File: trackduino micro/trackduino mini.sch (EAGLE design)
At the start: 28 parts, among them IC2 74AHC1G125DBV, SW1 SPST_TACT-KMR2, U1 ATMEGA168, Y1 16MHZ

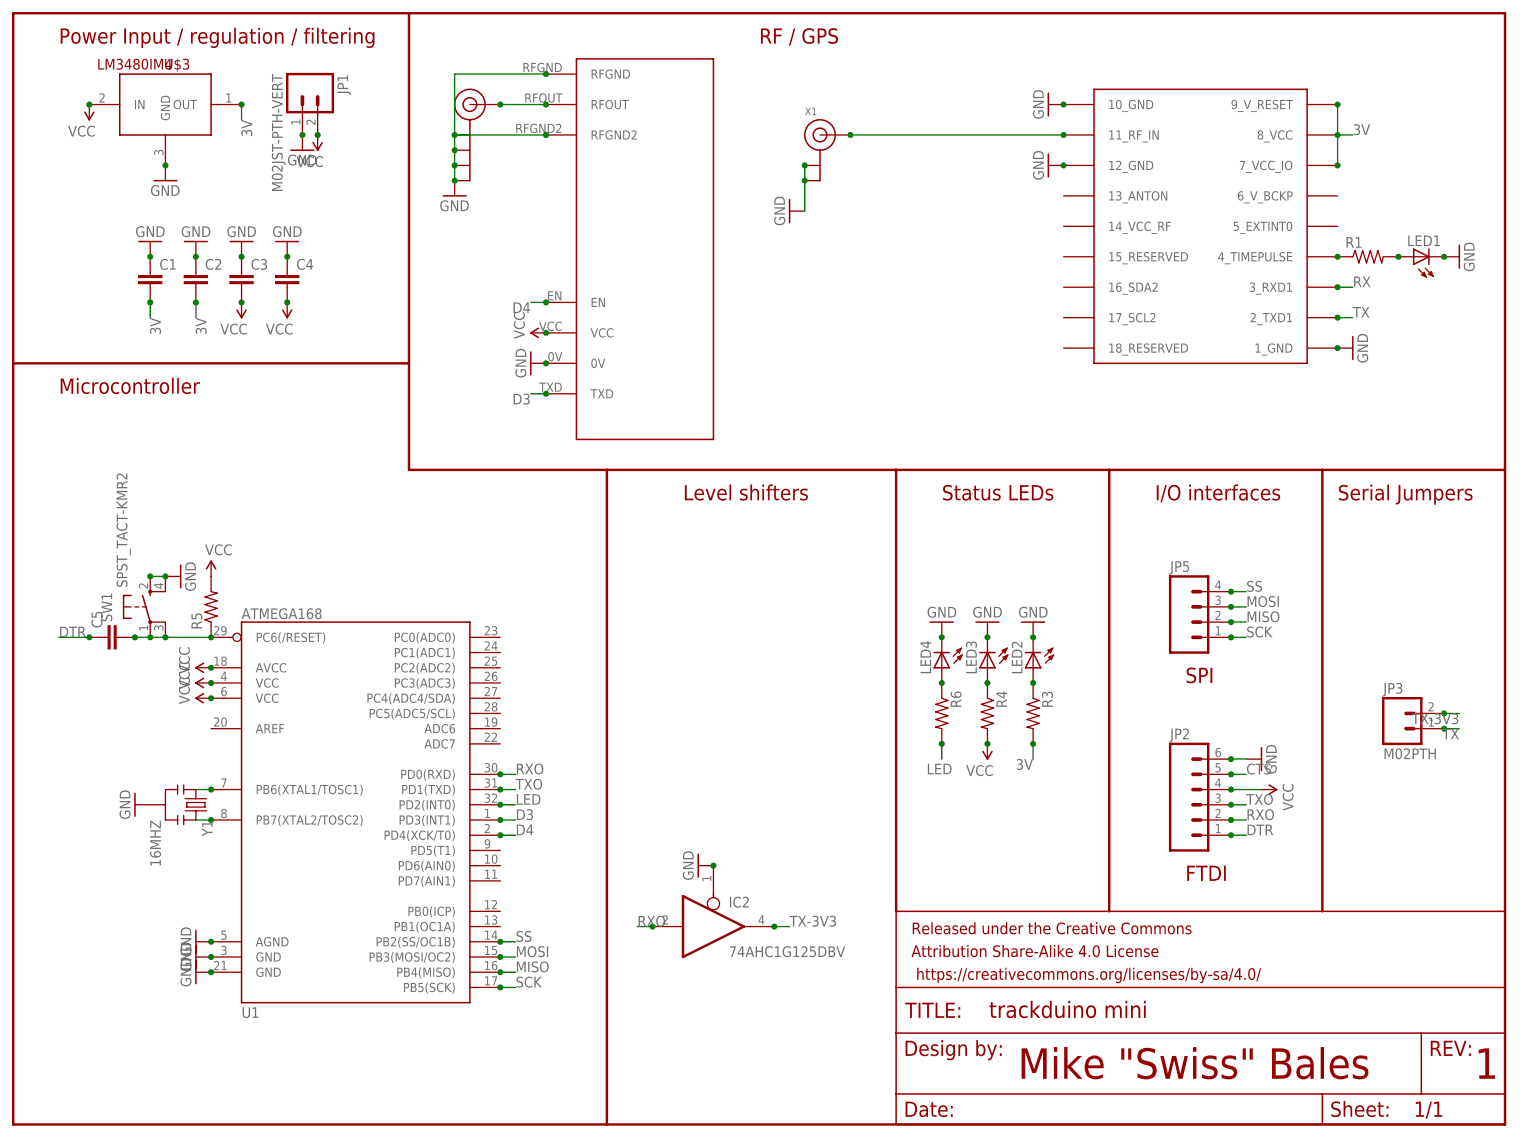
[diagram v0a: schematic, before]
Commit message: Revert 8864008..107cc9b
This rolls back to commit 8864008ccbdc4df3da8dbd79e6a63e8a5caf342f.
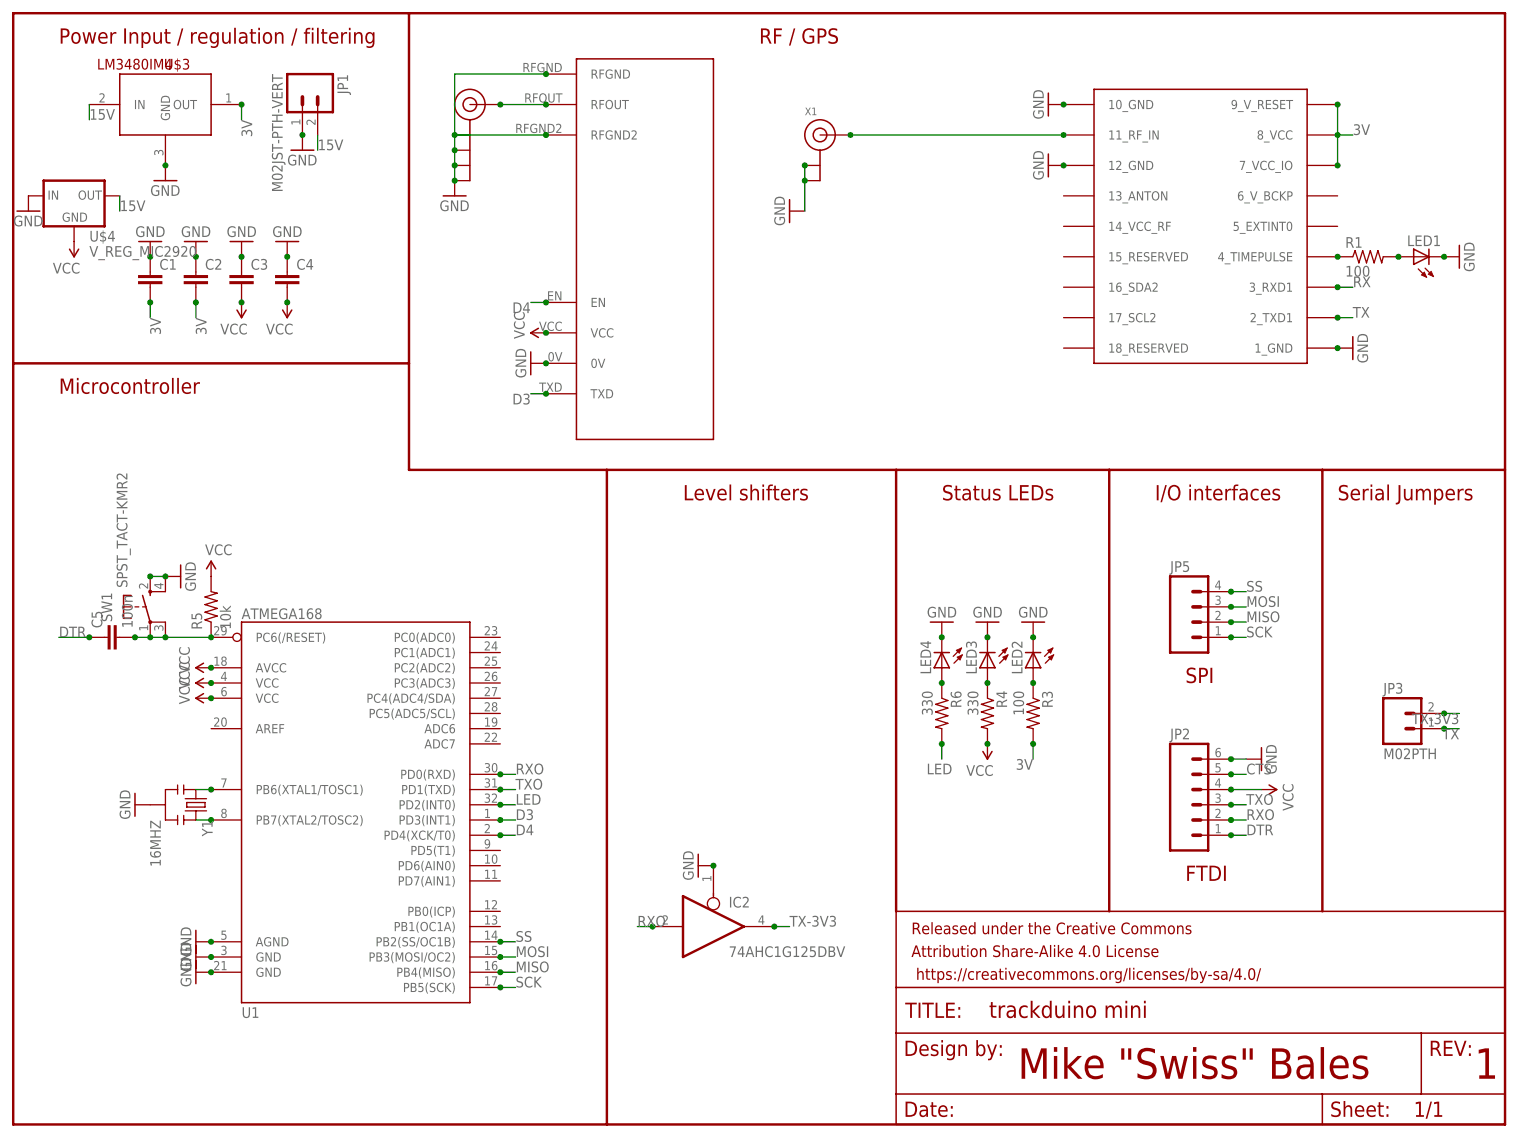
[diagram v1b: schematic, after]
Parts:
- added U$4: V_REG_MIC2920, SparkFun-PowerIC:V_REG_MIC2920
- C5: value (none) -> 100n
- R1, R3: value (none) -> 100
- R4, R6: value (none) -> 330
- R5: value (none) -> 10k
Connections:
- new net 15V: JP1.2, U$3.IN, U$4.OUT
- net GND: now also U$4.IN
- net VCC: now also U$4.GND; no longer JP1.2, U$3.IN
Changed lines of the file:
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@@
 <part name="GND4" library="SparkFun-Aesthetics" deviceset="GND" device=""/>
 <part name="GND5" library="SparkFun-Aesthetics" deviceset="GND" device=""/>
-<part name="SUPPLY1" library="SparkFun-Aesthetics" deviceset="VCC" device=""/>
-<part name="SUPPLY2" library="SparkFun-Aesthetics" deviceset="VCC" device=""/>
 <part name="SUPPLY3" library="SparkFun-Aesthetics" deviceset="VCC" device=""/>
 <part name="GND7" library="SparkFun-Aesthetics" deviceset="GND" device=""/>
-<part name="R1" library="SparkFun-Resistors" deviceset="RESISTOR" device="0805-RES"/>
+<part name="R1" library="SparkFun-Resistors" deviceset="RESISTOR" device="0805-RES" value="100"/>
 <part name="LED1" library="adafruit" deviceset="LED" device="CHIP-LED0805"/>
 <part name="GND8" library="SparkFun-Aesthetics" deviceset="GND" device=""/>
@@
 <part name="SUPPLY5" library="SparkFun-Aesthetics" deviceset="VCC" device=""/>
 <part name="LED2" library="adafruit" deviceset="LED" device="CHIP-LED0805"/>
-<part name="R3" library="SparkFun-Resistors" deviceset="RESISTOR" device="0805-RES"/>
+<part name="R3" library="SparkFun-Resistors" deviceset="RESISTOR" device="0805-RES" value="100"/>
 <part name="LED3" library="adafruit" deviceset="LED" device="CHIP-LED0805"/>
-<part name="R4" library="SparkFun-Resistors" deviceset="RESISTOR" device="0805-RES"/>
+<part name="R4" library="SparkFun-Resistors" deviceset="RESISTOR" device="0805-RES" value="330"/>
 <part name="GND19" library="SparkFun-Aesthetics" deviceset="GND" device=""/>
 <part name="GND20" library="SparkFun-Aesthetics" deviceset="GND" device=""/>
@@
 <part name="GND22" library="SparkFun-Aesthetics" deviceset="GND" device=""/>
 <part name="SUPPLY9" library="SparkFun-Aesthetics" deviceset="VCC" device=""/>
-<part name="R5" library="SparkFun-Resistors" deviceset="RESISTOR" device="0805-RES"/>
+<part name="R5" library="SparkFun-Resistors" deviceset="RESISTOR" device="0805-RES" value="10k"/>
 <part name="SUPPLY10" library="SparkFun-Aesthetics" deviceset="VCC" device=""/>
-<part name="C5" library="SparkFun-Capacitors" deviceset="CAP" device="0805"/>
+<part name="C5" library="SparkFun-Capacitors" deviceset="CAP" device="0805" value="100n"/>
 <part name="JP3" library="SparkFun-Connectors" deviceset="M02" device="PTH"/>
 <part name="JP5" library="SparkFun-Connectors" deviceset="M04" device="1X04_NO_SILK"/>
@@
 <part name="GND25" library="SparkFun-Aesthetics" deviceset="GND" device=""/>
 <part name="LED4" library="adafruit" deviceset="LED" device="CHIP-LED0805"/>
-<part name="R6" library="SparkFun-Resistors" deviceset="RESISTOR" device="0805-RES"/>
+<part name="R6" library="SparkFun-Resistors" deviceset="RESISTOR" device="0805-RES" value="330"/>
 <part name="GND26" library="SparkFun-Aesthetics" deviceset="GND" device=""/>
 <part name="GND24" library="SparkFun-Aesthetics" deviceset="GND" device=""/>
@@
 <part name="GND1" library="SparkFun-Aesthetics" deviceset="GND" device=""/>
 <part name="GND3" library="SparkFun-Aesthetics" deviceset="GND" device=""/>
+<part name="U$4" library="SparkFun-PowerIC" deviceset="V_REG_MIC2920" device=""/>
+<part name="SUPPLY12" library="SparkFun-Aesthetics" deviceset="VCC" device=""/>
+<part name="GND6" library="SparkFun-Aesthetics" deviceset="GND" device=""/>
 </parts>
 <sheets>
@@
 <instance part="GND4" gate="1" x="73.66" y="154.94"/>
 <instance part="GND5" gate="1" x="48.26" y="162.56"/>
-<instance part="SUPPLY1" gate="G$1" x="50.8" y="165.1" rot="R180"/>
-<instance part="SUPPLY2" gate="G$1" x="12.7" y="170.18" rot="R180"/>
 <instance part="SUPPLY3" gate="G$1" x="88.9" y="132.08" rot="R90"/>
 <instance part="GND7" gate="1" x="86.36" y="127" rot="R270"/>
@@
 <instance part="GND1" gate="1" x="30.48" y="147.32" rot="R180"/>
 <instance part="GND3" gate="1" x="25.4" y="157.48"/>
+<instance part="U$4" gate="G$1" x="10.16" y="154.94"/>
+<instance part="SUPPLY12" gate="G$1" x="10.16" y="147.32" rot="R180"/>
+<instance part="GND6" gate="1" x="2.54" y="152.4"/>
 </instances>
 <busses>
@@
 <junction x="25.4" y="160.02"/>
 </segment>
+<segment>
+<pinref part="U$4" gate="G$1" pin="IN"/>
+<pinref part="GND6" gate="1" pin="GND"/>
+</segment>
 </net>
 <net name="TX-3V3" class="0">
@@
 <net name="VCC" class="0">
 <segment>
-<pinref part="U$3" gate="G$1" pin="IN"/>
-<pinref part="SUPPLY2" gate="G$1" pin="VCC"/>
-<junction x="12.7" y="170.18"/>
-</segment>
-<segment>
-<pinref part="JP1" gate="G$1" pin="2"/>
-<pinref part="SUPPLY1" gate="G$1" pin="VCC"/>
-<junction x="50.8" y="165.1"/>
-</segment>
-<segment>
 <pinref part="U$2" gate="G$1" pin="VCC"/>
 <pinref part="SUPPLY3" gate="G$1" pin="VCC"/>
@@
 <pinref part="SUPPLY11" gate="G$1" pin="VCC"/>
 <junction x="33.02" y="76.2"/>
+</segment>
+<segment>
+<pinref part="U$4" gate="G$1" pin="GND"/>
+<pinref part="SUPPLY12" gate="G$1" pin="VCC"/>
 </segment>
 </net>
@@
 </segment>
 </net>
+<net name="15V" class="0">
+<segment>
+<pinref part="U$3" gate="G$1" pin="IN"/>
+<wire x1="12.7" y1="170.18" x2="12.7" y2="167.64" width="0.1524" layer="91"/>
+<label x="12.7" y="167.64" size="1.778" layer="95"/>
+</segment>
+<segment>
+<pinref part="JP1" gate="G$1" pin="2"/>
+<wire x1="50.8" y1="165.1" x2="50.8" y2="162.56" width="0.1524" layer="91"/>
+<label x="50.8" y="162.56" size="1.778" layer="95"/>
+</segment>
+<segment>
+<pinref part="U$4" gate="G$1" pin="OUT"/>
+<wire x1="17.78" y1="154.94" x2="17.78" y2="152.4" width="0.1524" layer="91"/>
+<label x="17.78" y="152.4" size="1.778" layer="95"/>
+</segment>
+</net>

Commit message: trackuino rev1
Fixed errors found after assembling the first prototype
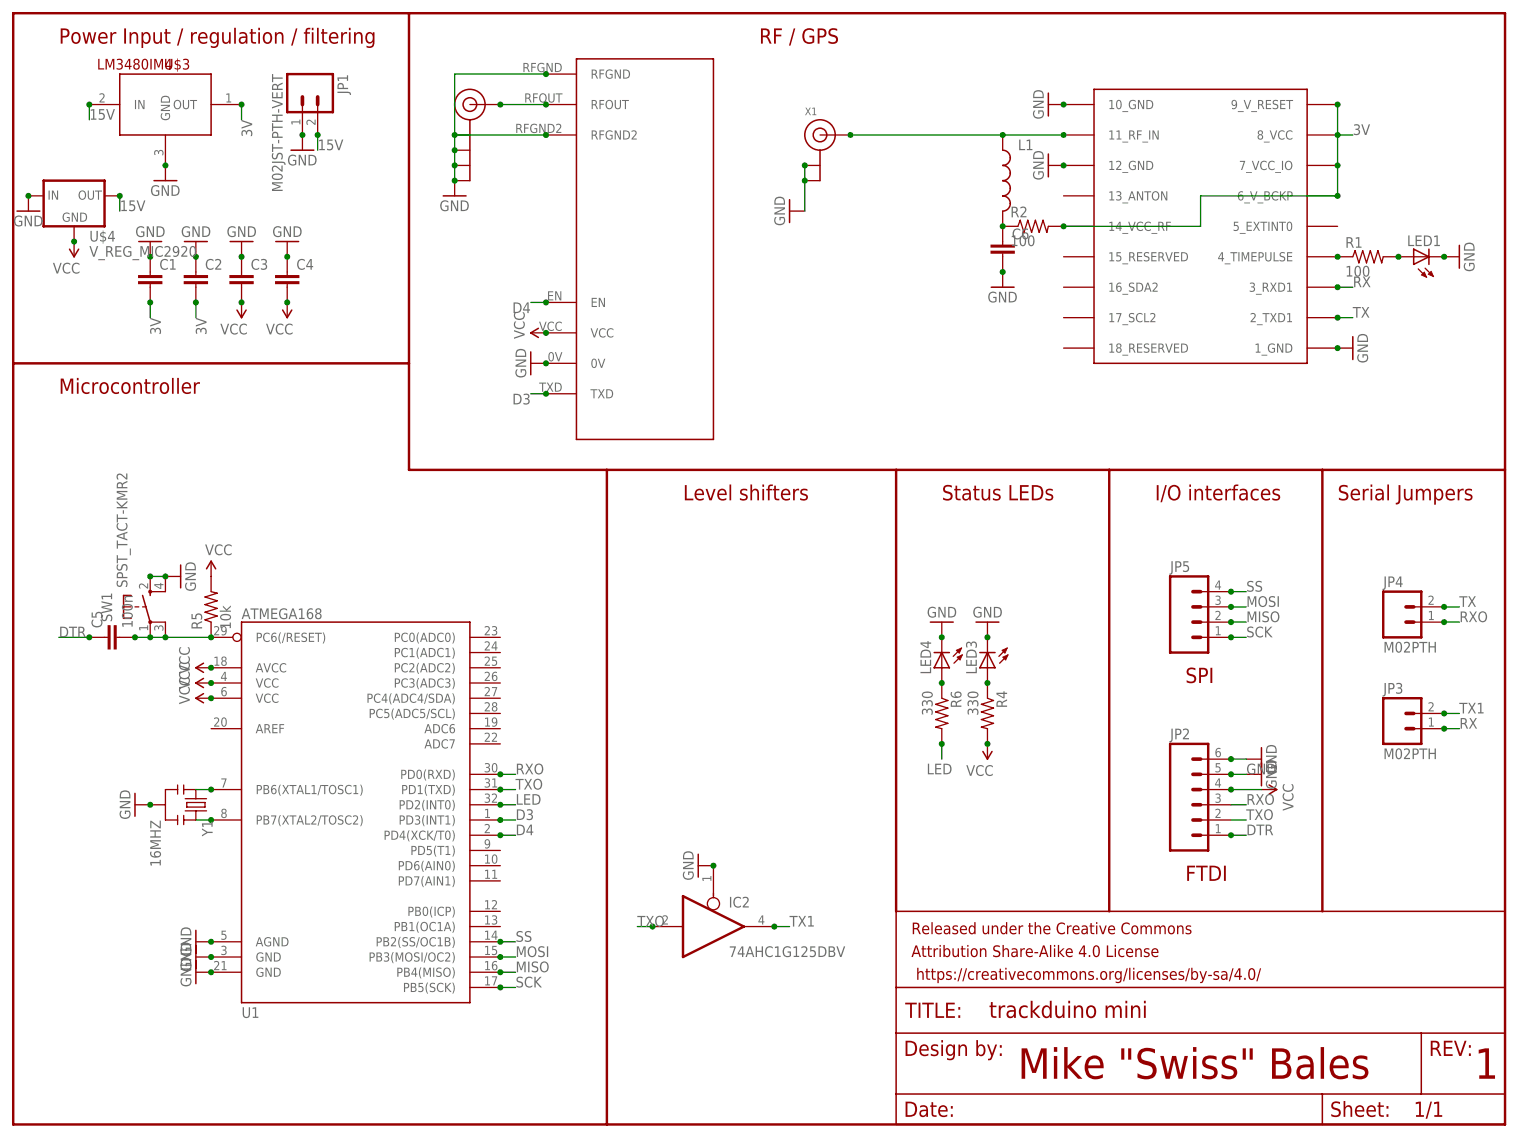
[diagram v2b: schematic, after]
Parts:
- removed LED2: (no value), adafruit:LEDCHIP-LED0805
- removed R3: 100, SparkFun-Resistors:RESISTOR0805-RES
- added C6: (no value), SparkFun-Capacitors:CAP0805
- added JP4: M02PTH, SparkFun-Connectors:M02PTH
- added L1: (no value), SparkFun-Passives:INDUCTOR0805
- added R2: 100, SparkFun-Resistors:RESISTOR0805-RES
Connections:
- net TX-3V3 renamed TX1
- removed net CTS: JP2.5
- removed net N$7: LED2.A, R3.1
- new net N$24: C6.1, L1.2, R2.1
- net 3V: now also R2.2, U$1.14_VCC_RF, U$1.6_V_BCKP; no longer R3.2
- net GND: now also C6.2, JP2.5; no longer LED2.C
- net N$6: now also L1.1
- net RX: now also JP3.1
- net RXO: now also JP2.3, JP4.1; no longer IC2A.I, JP2.2
- net TX: now also JP4.2; no longer JP3.1
- net TXO: now also IC2A.I, JP2.2; no longer JP2.3
